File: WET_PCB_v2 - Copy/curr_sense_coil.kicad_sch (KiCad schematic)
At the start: 9 parts, among them J17 Capacitor connector, U1 Opamp_Quad

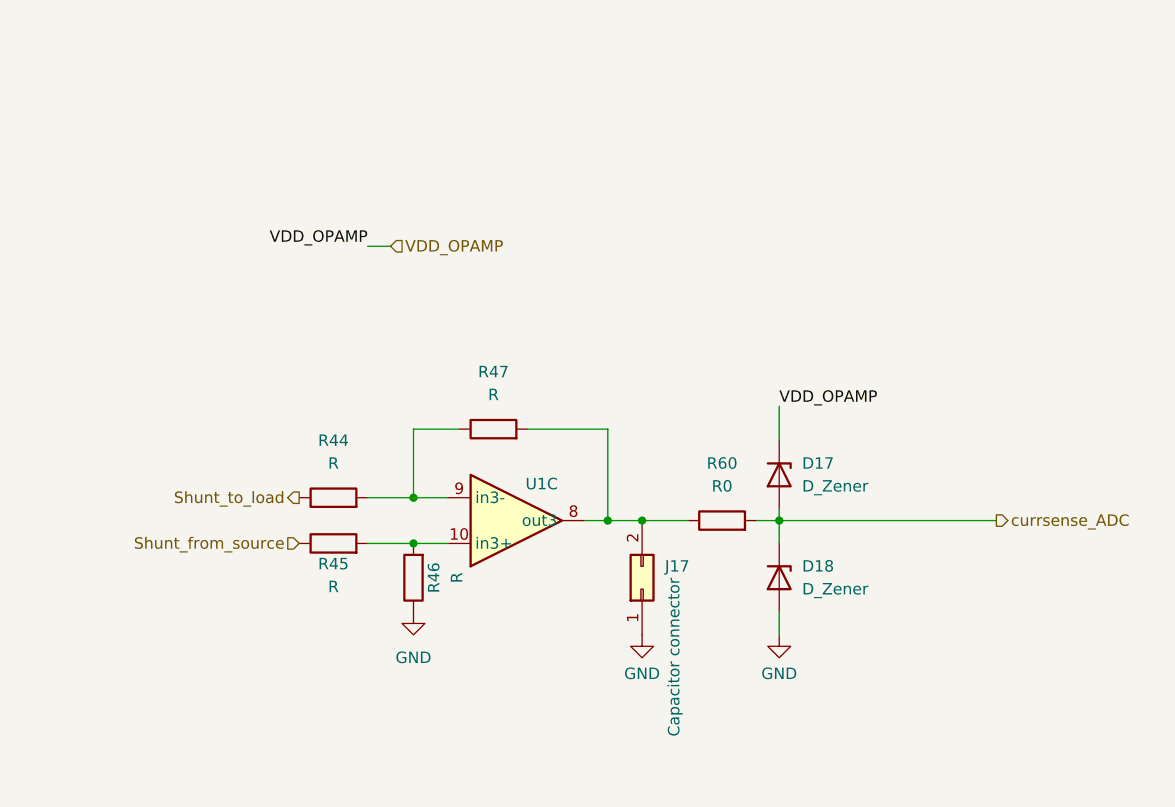
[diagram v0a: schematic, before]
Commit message: microcontroller to chip traces done
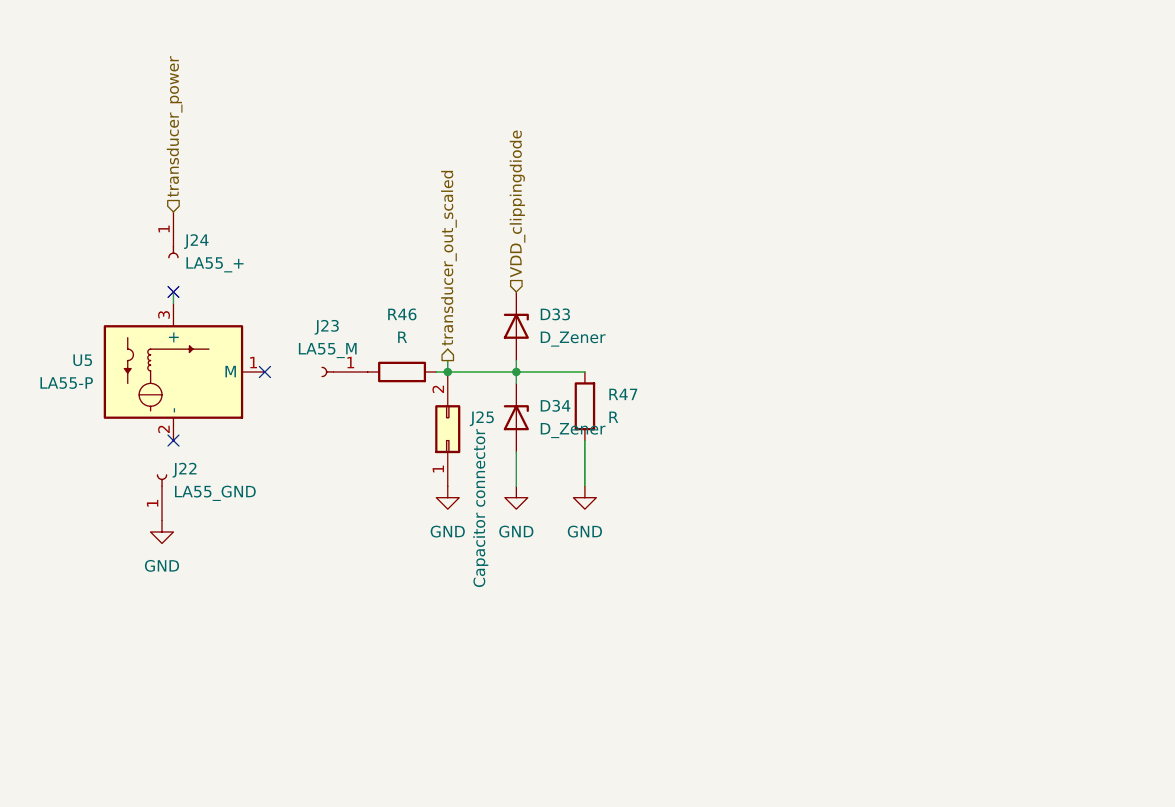
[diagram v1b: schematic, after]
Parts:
- removed D17, D18: D_Zener, Diode_SMD:D_SMF, symbol Device:D_Zener
- removed J17: Capacitor connector, Connector_PinSocket_2.54mm:PinSocket_1x02_P2.54mm_Horizontal, symbol Connector_Generic:Conn_02x01
- removed R44, R45: R, Resistor_SMD:R_0805_2012Metric_Pad1.20x1.40mm_HandSolder, symbol Device:R
- removed R60: R0, Resistor_SMD:R_0805_2012Metric_Pad1.20x1.40mm_HandSolder, symbol Device:R
- removed U1: Opamp_Quad, Package_DIP:DIP-14_W7.62mm, symbol Device:Opamp_Quad
- added D33, D34: D_Zener, Diode_THT:D_DO-15_P2.54mm_Vertical_CathodeUp, symbol Device:D_Zener
- added J22: LA55_GND, Connector_PinSocket_2.54mm:PinSocket_1x01_P2.54mm_Horizontal, symbol Connector:Conn_01x01_Socket
- added J23: LA55_M, Connector_PinSocket_2.54mm:PinSocket_1x01_P2.54mm_Horizontal, symbol Connector:Conn_01x01_Socket
- added J24: LA55_+, Connector_PinSocket_2.54mm:PinSocket_1x01_P2.54mm_Horizontal, symbol Connector:Conn_01x01_Socket
- added J25: Capacitor connector, Connector_PinSocket_2.54mm:PinSocket_1x02_P2.54mm_Vertical, symbol Connector_Generic:Conn_02x01
- added U5: LA55-P, Sensor_Current:LEM_LA25-P, symbol Sensor_Current:LA55-P
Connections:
- net GND: now also R47.1, D34.2 (A), J22.1 (Pin_1), J25.1 (Pin_1); no longer R46.1
- net transducer_out_scaled: now reaches R46.2
- net transducer_out_scaled: now also R47.2, D33.2 (A), D34.1 (K), J25.2 (Pin_2)
- new net: J23.1 (Pin_1), R46.1
- new net VDD_clippingdiode: D33.1 (K)
- new net transducer_power: J24.1 (Pin_1)
- no-connect marks 0 -> 3
